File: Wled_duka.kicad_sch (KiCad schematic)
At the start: 40 parts, among them J1 7775-2, J2 DATA channels, J3 CH1&2, J4 CH3&4, J5 Relay out, J6 DMX512, J7 7775-2, J8 3522-2, Q1 AO3400A, U1 XL1509-5.0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

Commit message: V2
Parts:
- removed J8: 3522-2, 35222, symbol keystone_3522-2:3522-2
- added J8: Vin_alt, Connector_PinHeader_2.54mm:PinHeader_1x02_P2.54mm_Vertical, symbol Connector:Conn_01x02_Pin
- F1, F2, F3, F4: footprint fusebox:35222 -> Keystone_fusebox:35222
- J1, J7: footprint 77752 -> Keystone_77752
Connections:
- net GND: now also J8.1 (Pin_1); no longer J7.2, J7.3, J7.4, J7.MH1
- net Vin: now also J1.1, J8.2 (Pin_2)
- no-connect marks 2 -> 7
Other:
- note added: "BUS_R 33-200 ohm"
- note added: "Channels"
- note added: "Fuses"
- note added: "LDO Vin(9-24V)-->5V"
- note added: "Mounting holes"
- note added: "Opcional"
- note added: "Power Relay Driver"
- note added: "Protection"
- note added: "Use ~5A fuse/channel"
- note removed: "Fuse"
- note removed: "LDO Vin-->5V-->3,3V"
- note removed: "Power Relay"
- moved on the sheet: D2, F3, F4, J2, TH1

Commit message: LDO
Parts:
- D3, D5: Mouser Part Number (none) -> 576-SMF12A
- F1, F2, F3, F4: Mouser Part Number (none) -> 534-3522-2
- J1, J7: Mouser Part Number 534-7775-2 -> 534-7775
- U2: now left out of the parts list
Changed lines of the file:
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@@
 			)
 		)
+		(property "Mouser Part Number" "576-SMF12A"
+			(at 167.64 49.53 90)
+			(hide yes)
+			(show_name no)
+			(do_not_autoplace no)
+			(effects
+				(font
+					(size 1.27 1.27)
+				)
+			)
+		)
 		(pin "1"
 		)
@@
 			)
 		)
+		(property "Mouser Part Number" "534-3522-2"
+			(at 46.99 104.14 0)
+			(hide yes)
+			(show_name no)
+			(do_not_autoplace no)
+			(effects
+				(font
+					(size 1.27 1.27)
+				)
+			)
+		)
 		(pin "2"
 		)
@@
 		(body_style 1)
 		(exclude_from_sim no)
-		(in_bom yes)
+		(in_bom no)
 		(on_board yes)
 		(in_pos_files yes)
@@
 			)
 		)
+		(property "Mouser Part Number" "534-3522-2"
+			(at 29.21 104.14 0)
+			(hide yes)
+			(show_name no)
+			(do_not_autoplace no)
+			(effects
+				(font
+					(size 1.27 1.27)
+				)
+			)
+		)
 		(pin "2"
 		)
@@
 			)
 		)
-		(property "Mouser Part Number" "534-7775-2"
+		(property "Mouser Part Number" "534-7775"
 			(at 217.17 615.57 0)
 			(hide yes)
@@
 			)
 		)
+		(property "Mouser Part Number" "534-3522-2"
+			(at 38.1 104.14 0)
+			(hide yes)
+			(show_name no)
+			(do_not_autoplace no)
+			(effects
+				(font
+					(size 1.27 1.27)
+				)
+			)
+		)
 		(pin "2"
 		)
@@
 			)
 		)
+		(property "Mouser Part Number" "534-3522-2"
+			(at 19.05 104.14 0)
+			(hide yes)
+			(show_name no)
+			(do_not_autoplace no)
+			(effects
+				(font
+					(size 1.27 1.27)
+				)
+			)
+		)
 		(pin "2"
 		)
@@
 			)
 		)
+		(property "Mouser Part Number" "576-SMF12A"
+			(at 156.21 50.8 90)
+			(hide yes)
+			(show_name no)
+			(do_not_autoplace no)
+			(effects
+				(font
+					(size 1.27 1.27)
+				)
+			)
+		)
 		(pin "1"
 		)
@@
 			)
 		)
-		(property "Mouser Part Number" "534-7775-2"
+		(property "Mouser Part Number" "534-7775"
 			(at 218.44 620.65 0)
 			(hide yes)

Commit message: GND fix
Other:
- moved on the sheet: J3
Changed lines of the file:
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@@
 	(rectangle
 		(start 13.97 151.13)
-		(end 142.24 191.77)
+		(end 142.24 189.23)
 		(stroke
 			(width 0)
@@
 	(wire
 		(pts
-			(xy 21.59 119.38) (xy 21.59 123.19)
+			(xy 21.59 119.38) (xy 21.59 121.92)
 		)
 		(stroke
@@
 	(wire
 		(pts
-			(xy 19.05 107.95) (xy 19.05 123.19)
+			(xy 19.05 107.95) (xy 19.05 121.92)
 		)
 		(stroke
@@
 	(wire
 		(pts
-			(xy 24.13 107.95) (xy 24.13 123.19)
+			(xy 24.13 107.95) (xy 24.13 121.92)
 		)
 		(stroke
@@
 	(wire
 		(pts
-			(xy 26.67 119.38) (xy 26.67 123.19)
+			(xy 26.67 119.38) (xy 26.67 121.92)
 		)
 		(stroke
@@
 	(symbol
 		(lib_id "Connector:Screw_Terminal_01x04")
-		(at 24.13 128.27 270)
+		(at 24.13 127 270)
 		(unit 1)
 		(body_style 1)
@@
 		(dnp no)
 		(property "Reference" "J3"
-			(at 22.86 132.08 90)
+			(at 22.86 130.81 90)
 			(show_name no)
 			(do_not_autoplace no)
@@
 		)
 		(property "Value" "CH1&2"
-			(at 22.86 134.62 90)
+			(at 22.86 133.35 90)
 			(show_name no)
 			(do_not_autoplace no)
@@
 		)
 		(property "Footprint" "TerminalBlock_Ningbo-Kagnex:TerminalBlock_Ningbo-Kagnex_HB9500_1x04_P9.5mm"
-			(at 24.13 128.27 0)
+			(at 24.13 127 0)
 			(hide yes)
 			(show_name no)
@@
 		)
 		(property "Datasheet" ""
-			(at 24.13 128.27 0)
+			(at 24.13 127 0)
 			(hide yes)
 			(show_name no)
@@
 		)
 		(property "Description" "Generic screw terminal, single row, 01x04, script generated (kicad-library-utils/schlib/autogen/connector/)"
-			(at 24.13 128.27 0)
+			(at 24.13 127 0)
 			(hide yes)
 			(show_name no)

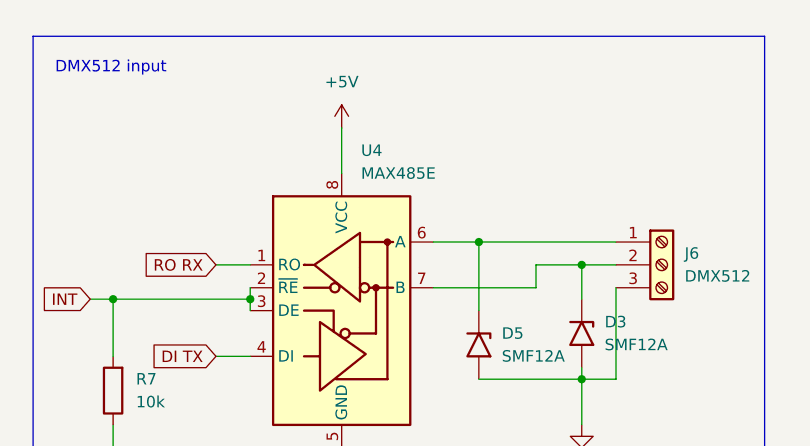
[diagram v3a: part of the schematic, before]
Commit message: Max485 remove --- Max3485 placed
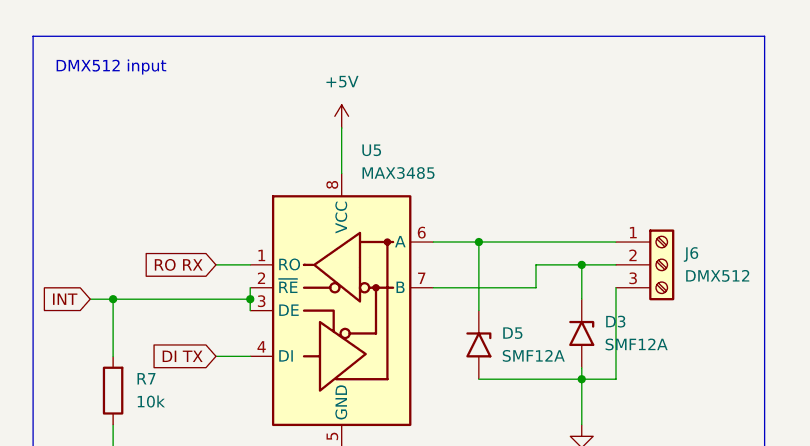
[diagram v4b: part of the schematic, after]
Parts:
- removed U4: MAX485E, Package_SO:SOIC-8_3.9x4.9mm_P1.27mm, symbol Interface_UART:MAX485E
- added U5: MAX3485, Package_SO:SOIC-8_3.9x4.9mm_P1.27mm, symbol Interface_UART:MAX3485
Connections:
- net +5V: now also U5.8 (VCC)
- net DI TX: now also U5.4 (DI)
- net GND: now also U5.5 (GND)
- net INT: now also U5.2 (~{RE}), U5.3 (DE)
- net RO RX: now also U5.1 (RO)
- net at D3.1 (A1), J6.2 (Pin_2): now also U5.7 (B)
- net at D5.1 (A1), J6.1 (Pin_1): now also U5.6 (A)
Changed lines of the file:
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@@
 	)
 	(symbol
-		(lib_id "Interface_UART:MAX485E")
-		(at 140.97 46.99 0)
-		(unit 1)
-		(body_style 1)
-		(exclude_from_sim no)
-		(in_bom yes)
-		(on_board yes)
-		(in_pos_files yes)
-		(dnp no)
-		(fields_autoplaced yes)
-		(property "Reference" "U4"
-			(at 143.1133 29.21 0)
-			(show_name no)
-			(do_not_autoplace no)
-			(effects
-				(font
-					(size 1.27 1.27)
-				)
-				(justify left)
-			)
-		)
-		(property "Value" "MAX485E"
-			(at 143.1133 31.75 0)
-			(show_name no)
-			(do_not_autoplace no)
-			(effects
-				(font
-					(size 1.27 1.27)
-				)
-				(justify left)
-			)
-		)
-		(property "Footprint" "Package_SO:SOIC-8_3.9x4.9mm_P1.27mm"
-			(at 140.97 69.85 0)
-			(hide yes)
-			(show_name no)
-			(do_not_autoplace no)
-			(effects
-				(font
-					(size 1.27 1.27)
-				)
-			)
-		)
-		(property "Datasheet" "https://datasheets.maximintegrated.com/en/ds/MAX1487E-MAX491E.pdf"
-			(at 140.97 45.72 0)
-			(hide yes)
-			(show_name no)
-			(do_not_autoplace no)
-			(effects
-				(font
-					(size 1.27 1.27)
-				)
-			)
-		)
-		(property "Description" "Half duplex RS-485/RS-422, 2.5 Mbps, ±15kV electro-static discharge (ESD) protection, no slew-rate, no low-power shutdown, with receiver/driver enable, 32 receiver drive capability, DIP-8 and SOIC-8"
-			(at 140.97 46.99 0)
-			(hide yes)
-			(show_name no)
-			(do_not_autoplace no)
-			(effects
-				(font
-					(size 1.27 1.27)
-				)
-			)
-		)
-		(pin "4"
-		)
-		(pin "3"
-		)
-		(pin "2"
-		)
-		(pin "6"
-		)
-		(pin "5"
-		)
-		(pin "8"
-		)
-		(pin "1"
-		)
-		(pin "7"
-		)
-		(instances
-			(project "Wled_duka"
-				(path "/120a8a38-e990-43f6-ba11-7662a7c27749"
-					(reference "U4")
-					(unit 1)
-				)
-			)
-		)
-	)
-	(symbol
 		(lib_id "Regulator_Switching:XL1509-5.0")
 		(at 55.88 167.64 0)
@@
 					(unit 1)
 				)
+			)
+		)
+	)
+	(symbol
+		(lib_id "Interface_UART:MAX3485")
+		(at 140.97 46.99 0)
+		(unit 1)
+		(body_style 1)
+		(exclude_from_sim no)
+		(in_bom yes)
+		(on_board yes)
+		(in_pos_files yes)
+		(dnp no)
+		(fields_autoplaced yes)
+		(property "Reference" "U5"
+			(at 143.1133 29.21 0)
+			(show_name no)
+			(do_not_autoplace no)
+			(effects
+				(font
+					(size 1.27 1.27)
+				)
+				(justify left)
+			)
+		)
+		(property "Value" "MAX3485"
+			(at 143.1133 31.75 0)
+			(show_name no)
+			(do_not_autoplace no)
+			(effects
+				(font
+					(size 1.27 1.27)
+				)
+				(justify left)
+			)
+		)
+		(property "Footprint" "Package_SO:SOIC-8_3.9x4.9mm_P1.27mm"
+			(at 140.97 69.85 0)
+			(hide yes)
+			(show_name no)
+			(do_not_autoplace no)
+			(effects
+				(font
+					(size 1.27 1.27)
+				)
+			)
+		)
+		(property "Datasheet" "https://datasheets.maximintegrated.com/en/ds/MAX3483-MAX3491.pdf"
+			(at 140.97 45.72 0)
+			(hide yes)
+			(show_name no)
+			(do_not_autoplace no)
+			(effects
+				(font
+					(size 1.27 1.27)
+				)
+			)
+		)
+		(property "Description" "True RS-485/RS-422, 10Mbps, Slew-Rate Limited, with low-power shutdown, with receiver/driver enable, 32 receiver drive capacitity, DIP-8 and SOIC-8"
+			(at 140.97 46.99 0)
+			(hide yes)
+			(show_name no)
+			(do_not_autoplace no)
+			(effects
+				(font
+					(size 1.27 1.27)
+				)
+			)
+		)
+		(pin "5"
+		)
+		(pin "7"
+		)
+		(pin "4"
+		)
+		(pin "6"
+		)
+		(pin "3"
+		)
+		(pin "2"
+		)
+		(pin "1"
+		)
+		(pin "8"
+		)
+		(instances
+			(project "Wled_duka"
+				(path "/120a8a38-e990-43f6-ba11-7662a7c27749"
+					(reference "U5")
+					(unit 1)
+				)

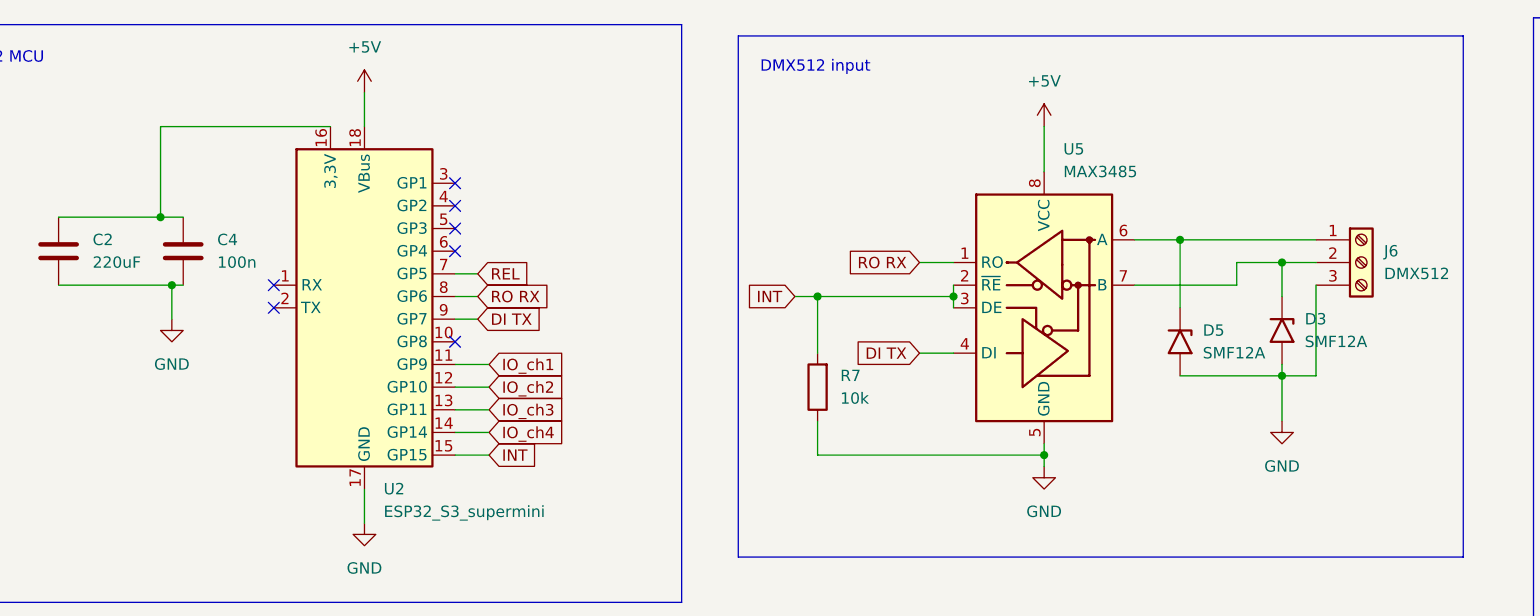
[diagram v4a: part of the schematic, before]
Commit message: Pullup and Pulldown resistors, 3,3V for max3485
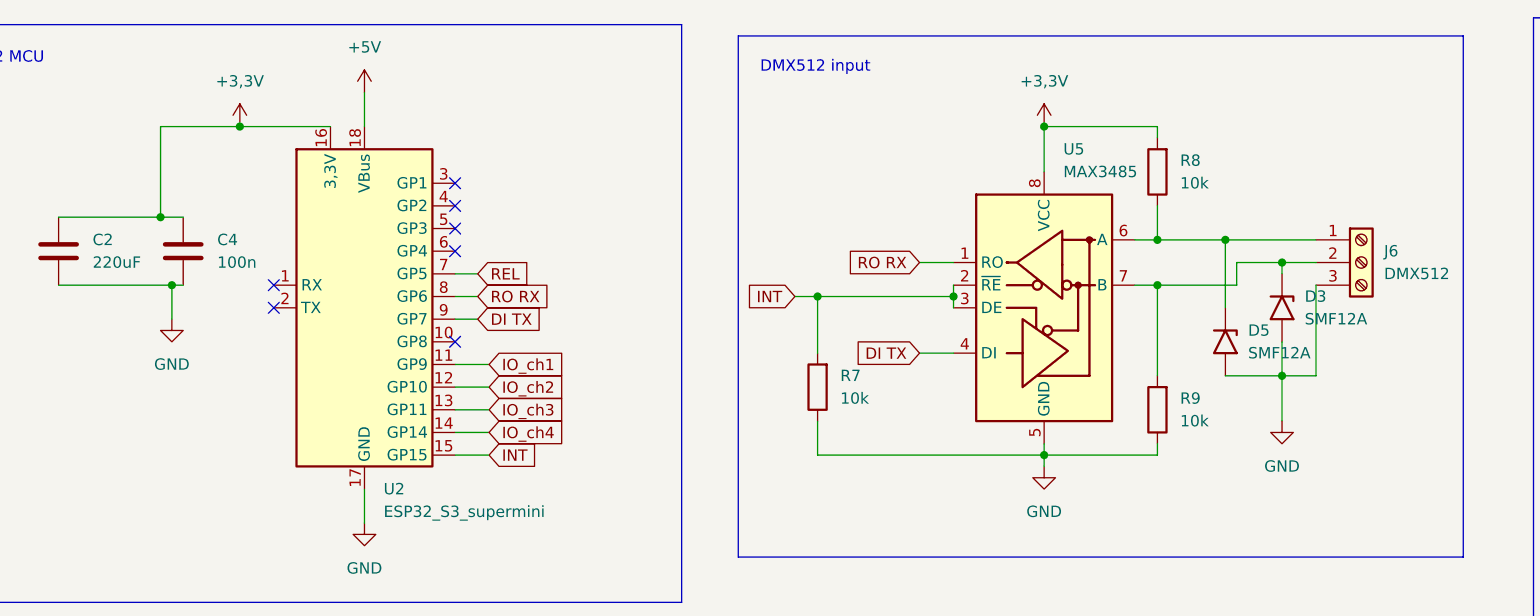
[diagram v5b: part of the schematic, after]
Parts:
- added R8, R9: 10k, Resistor_SMD:R_0805_2012Metric_Pad1.20x1.40mm_HandSolder, symbol Device:R
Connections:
- net +5V: no longer U5.8 (VCC)
- net GND: now also R9.1
- net at D3.1 (A1), J6.2 (Pin_2), U5.7 (B): now also R9.2
- net at D5.1 (A1), J6.1 (Pin_1), U5.6 (A): now also R8.1
- net +3,3V: now reaches C2.1, C4.1, U2.16 (3,3V)
- net +3,3V: now also U5.8 (VCC), R8.2
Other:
- moved on the sheet: D3, D5
